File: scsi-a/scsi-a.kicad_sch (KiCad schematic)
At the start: 17 parts, among them J1 Conn_02x25_Odd_Even, J3 Conn_02x08_Odd_Even, J4 Conn_02x08_Odd_Even, J5 DB25_Receptacle, J6 Conn_02x10_Counter_Clockwise, J7 Conn_02x10_Counter_Clockwise, Q1 BC547, U1 Z53C80003VSG, U2 74LS138, U3 74HC00

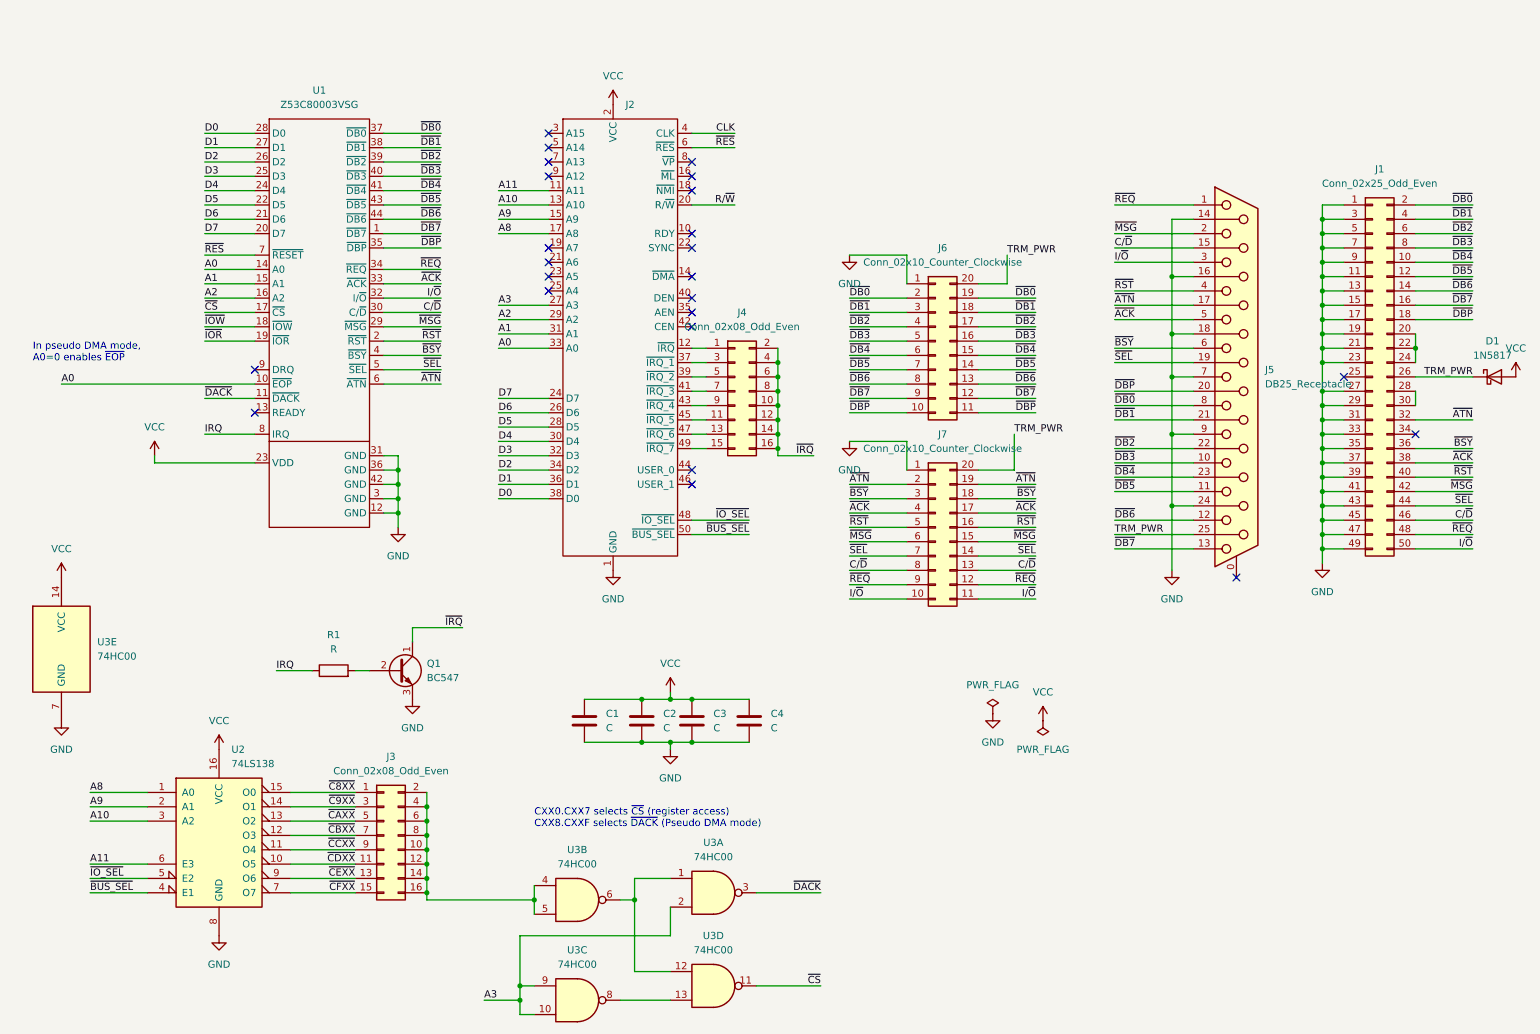
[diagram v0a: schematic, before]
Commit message: Minimal change to fix SCSI CPU-Bus connection
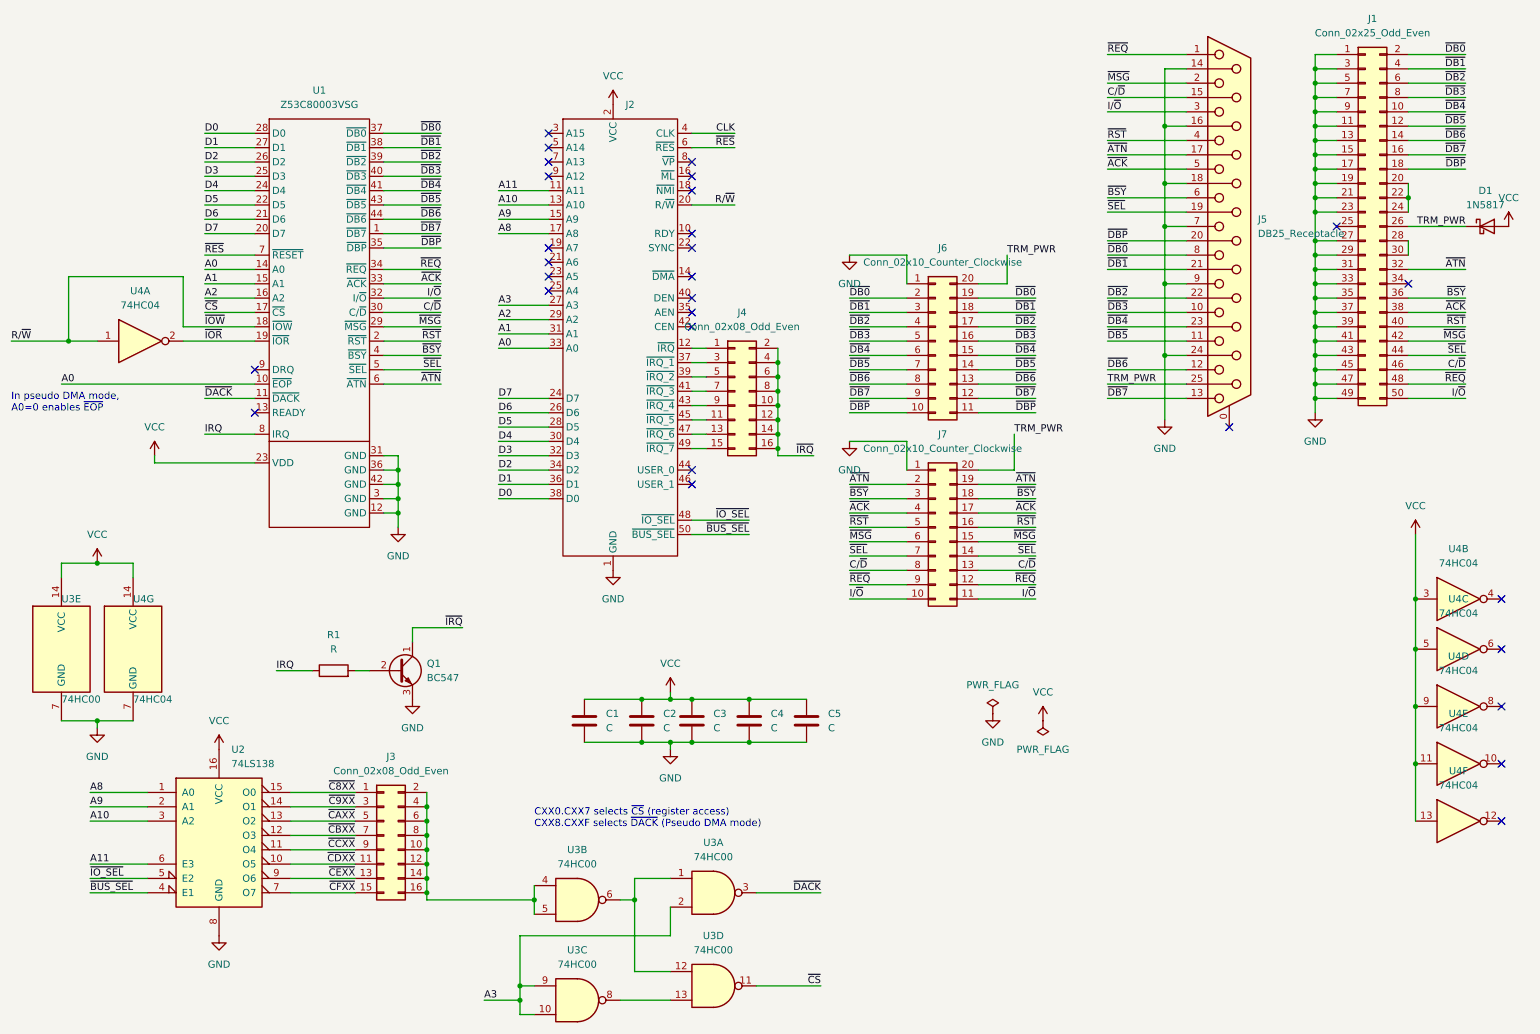
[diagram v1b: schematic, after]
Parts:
- added C5: C, Capacitor_THT:C_Disc_D5.0mm_W2.5mm_P5.00mm, symbol Device:C
- added U4: 74HC04, Package_DIP:DIP-14_W7.62mm, symbol 74xx:74AHC04
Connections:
- net ~{IOW} is gone; now on net R/~{W}: U1.18 (~{IOW})
- net GND: now also C5.2, U4.7 (GND)
- net R/~{W}: now also U4.1
- net VCC: now also C5.1, U4.11, U4.13, U4.14 (VCC), U4.3, U4.5, U4.9
- net ~{IOR}: now also U4.2
- no-connect marks 24 -> 29
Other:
- title: (none) -> FP65 SCSI-SC interface
- moved on the sheet: D1, J1, J5

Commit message: Fix DB footprint on SCSI-A and SIO-A
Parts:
- J5: footprint Connector_Dsub:DSUB-25_Female_Horizontal_P2.77x2.84mm_EdgePinOffset4.94mm_Housed_MountingHolesOffset7.48mm -> Connector_Dsub:DSUB-25_Female_Horizontal_P2.77x2.84mm_EdgePinOffset9.90mm_Housed_MountingHolesOffset11.32mm
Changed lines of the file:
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@@
       (effects (font (size 1.27 1.27)) (justify left))
     )
-    (property "Footprint" "Connector_Dsub:DSUB-25_Female_Horizontal_P2.77x2.84mm_EdgePinOffset4.94mm_Housed_MountingHolesOffset7.48mm" (at 229.87 54.61 0)
+    (property "Footprint" "Connector_Dsub:DSUB-25_Female_Horizontal_P2.77x2.84mm_EdgePinOffset9.90mm_Housed_MountingHolesOffset11.32mm" (at 229.87 54.61 0)
       (effects (font (size 1.27 1.27)) hide)
     )
